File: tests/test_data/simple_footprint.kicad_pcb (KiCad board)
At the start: 2 copper layers, 40 x 40 mm, 16 parts, among them J1 Conn, J1 SS52300001

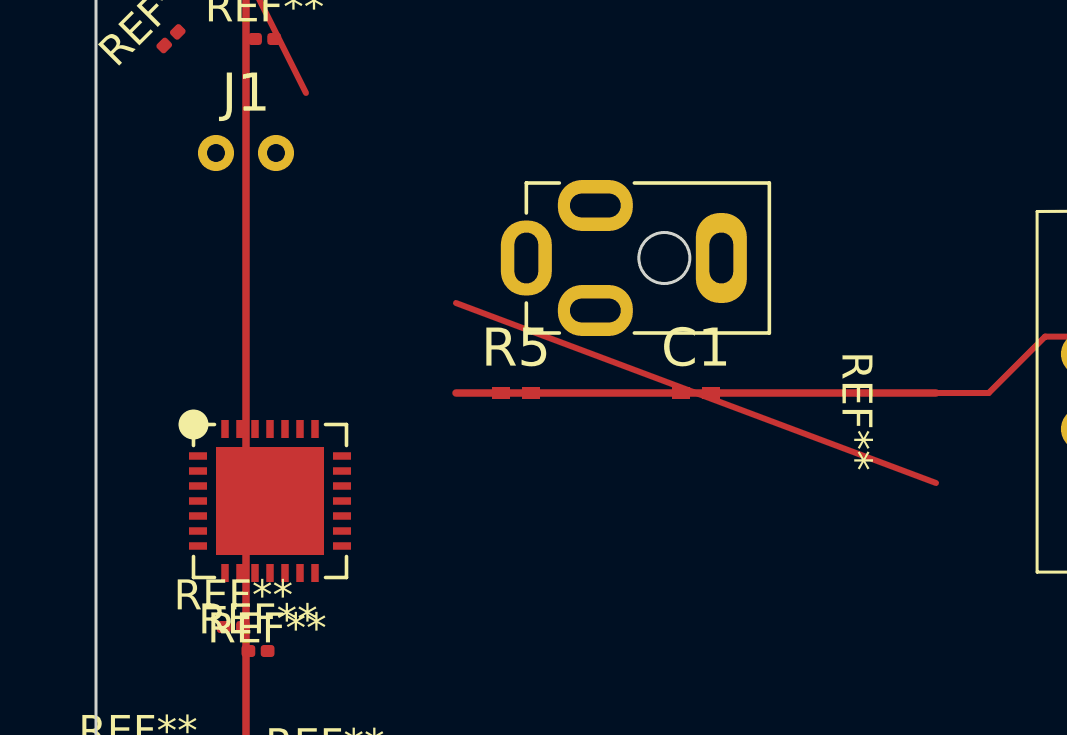
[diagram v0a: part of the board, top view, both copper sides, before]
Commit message: Update test data files for KiCad 10 format compatibility
KiCad 10 re-saved these files with regenerated UUIDs. All tests pass.
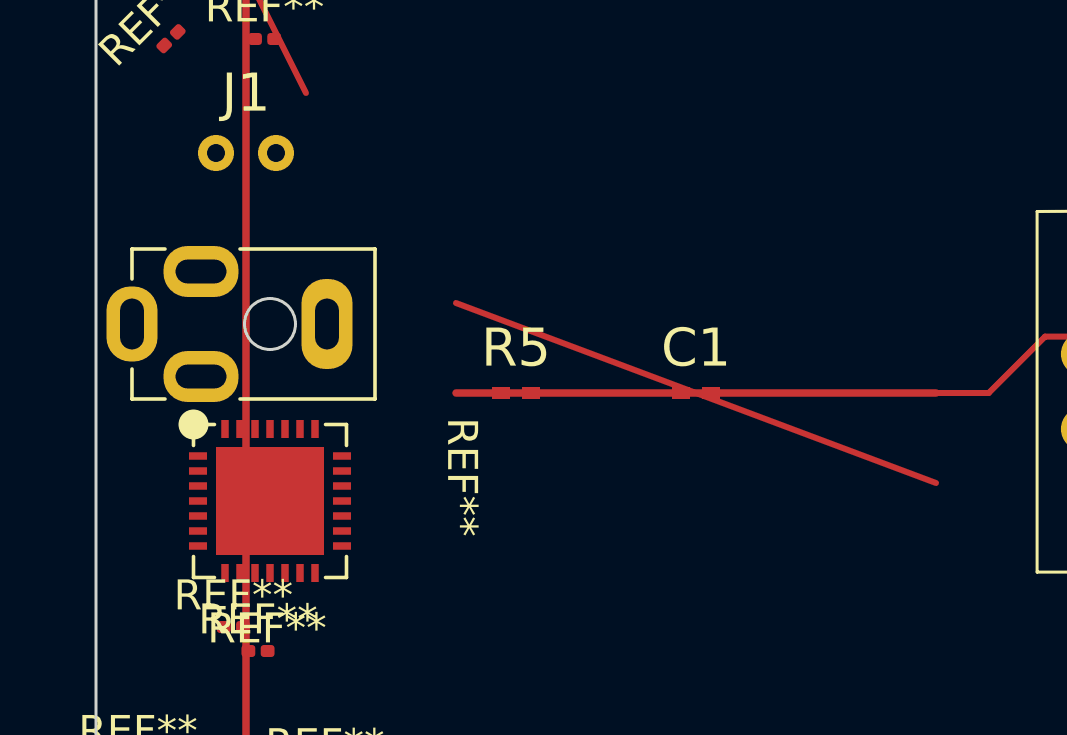
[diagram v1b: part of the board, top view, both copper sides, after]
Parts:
- moved REF** 13.3 mm to (9.30, 17.7)
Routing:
- net (no net): track 0.00 -> 40.3 mm
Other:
- copper layers 2 -> 4
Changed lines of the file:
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@@
 	(layers
 		(0 "F.Cu" signal)
+		(4 "In1.Cu" signal)
+		(6 "In2.Cu" signal)
 		(2 "B.Cu" signal)
 		(25 "Edge.Cuts" user)
@@
 	)
 	(setup
+		(stackup
+			(layer "F.Cu"
+				(type "copper")
+				(thickness 0.035)
+			)
+			(layer "dielectric 1"
+				(type "prepreg")
+				(thickness 0.02)
+				(material "FR4")
+				(epsilon_r 4.5)
+				(loss_tangent 0.02)
+			)
+			(layer "In1.Cu"
+				(type "copper")
+				(thickness 0.035)
+			)
+			(layer "dielectric 2"
+				(type "core")
+				(thickness 0.02)
+				(material "FR4")
+				(epsilon_r 4.5)
+				(loss_tangent 0.02)
+			)
+			(layer "In2.Cu"
+				(type "copper")
+				(thickness 0.035)
+			)
+			(layer "dielectric 3"
+				(type "prepreg")
+				(thickness 0.02)
+				(material "FR4")
+				(epsilon_r 4.5)
+				(loss_tangent 0.02)
+			)
+			(layer "B.Cu"
+				(type "copper")
+				(thickness 0.035)
+			)
+			(copper_finish "None")
+			(dielectric_constraints no)
+		)
 		(pad_to_mask_clearance 0)
 		(allow_soldermask_bridges_in_footprints no)
@@
 	(footprint "00_custom-footprints:Jack_Socket_PJ-210B"
 		(layer "F.Cu")
-		(at 22.445 15.5 -90)
+		(at 9.3 17.7 -90)
 		(descr "2.5mm Female Audio Connector 4 Pin DIP Headphone Jack Socket PJ-210B")
 		(tags "2.5mm Female Audio Jack")
@@
 	)
 	(segment
+		(start 32.88 21.2)
+		(end 11.2 21.2)
+		(width 0.2)
+		(layer "In1.Cu")
+		(net 0)
+	)
+	(segment
+		(start 12 15.5)
+		(end 20 15.5)
+		(width 0.2)
+		(layer "In1.Cu")
+		(net 0)
+	)
+	(segment
+		(start 8 11.5)
+		(end 12 15.5)
+		(width 0.2)
+		(layer "In1.Cu")
+		(net 0)
+	)
+	(segment
+		(start 11.2 21.2)
+		(end 7.7 17.7)
+		(width 0.2)
+		(layer "In1.Cu")
+		(net 0)
+	)
+	(segment
